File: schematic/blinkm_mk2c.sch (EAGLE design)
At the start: 16 parts, among them CN1 1X4SMT, U1 ATTINY44QFN

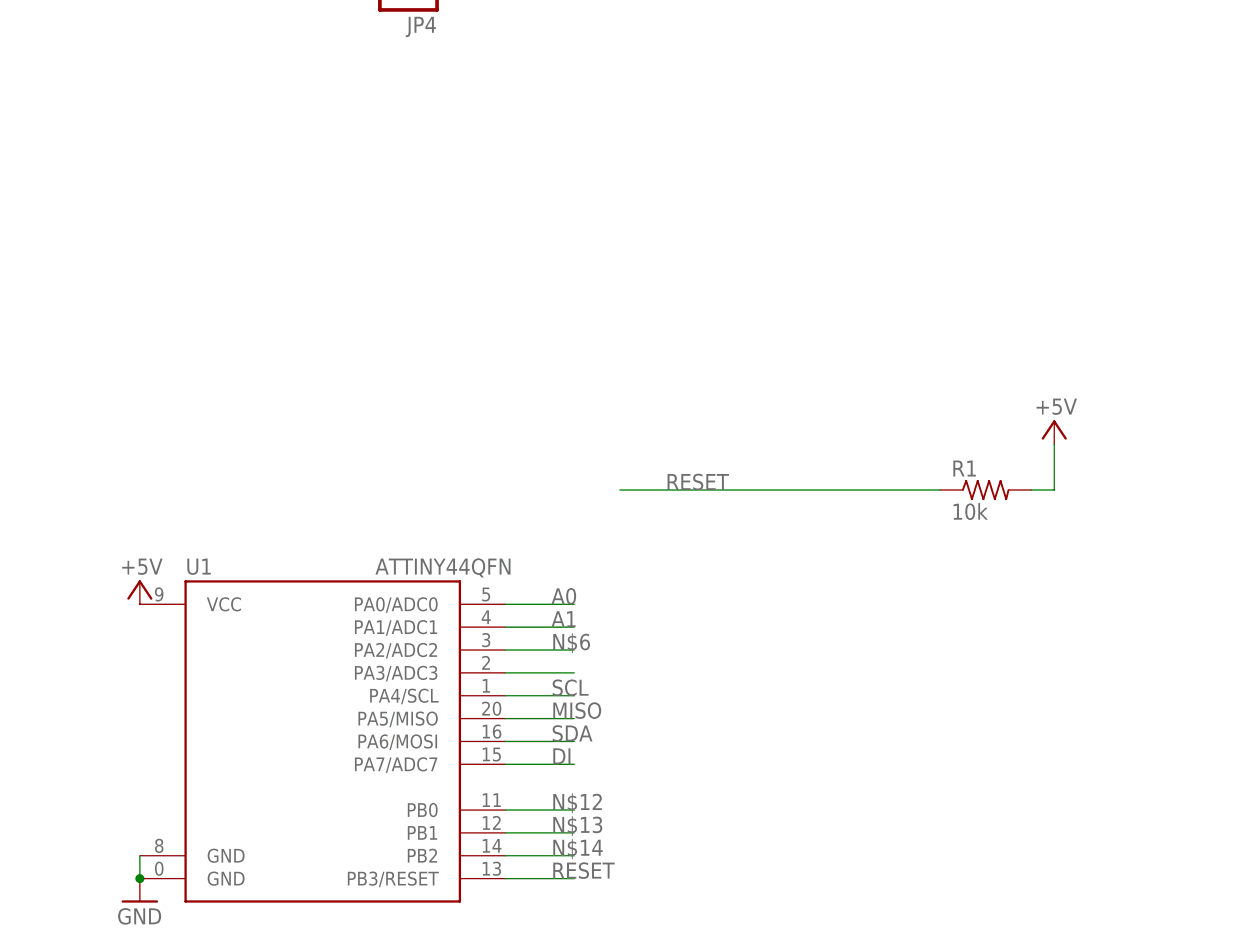
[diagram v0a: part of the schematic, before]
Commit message: updated blinkm_mk2c board layout, fully routed
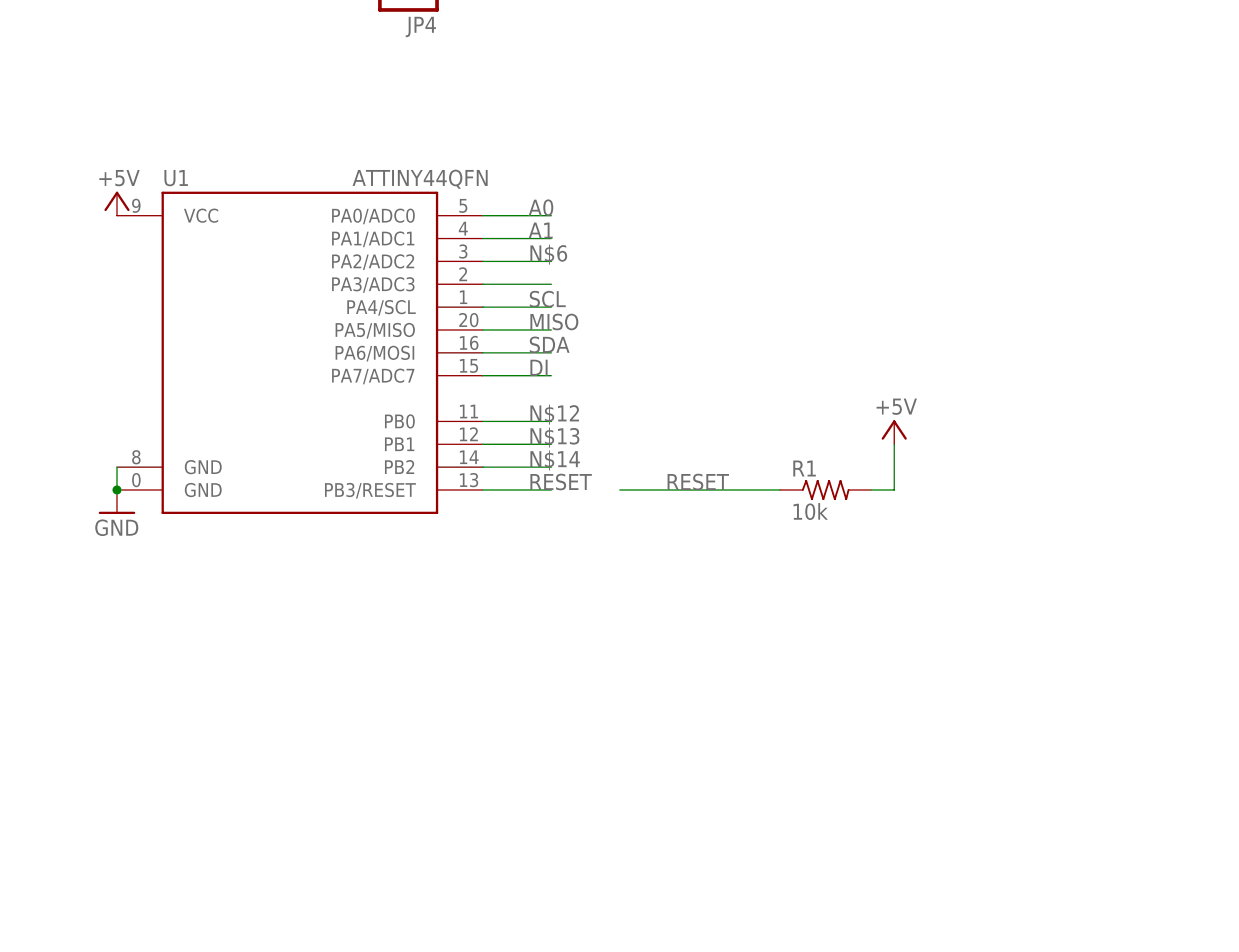
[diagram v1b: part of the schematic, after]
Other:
- moved on the sheet: R1, U1
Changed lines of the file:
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@@
 <instance part="C1" gate="G$1" x="22.86" y="175.26"/>
 <instance part="GND7" gate="1" x="220.98" y="83.82"/>
-<instance part="R1" gate="G$1" x="127" y="71.12"/>
-<instance part="P+3" gate="1" x="134.62" y="78.74" smashed="yes">
-<attribute name="VALUE" x="137.16" y="81.28" size="1.778" layer="96" rot="R180"/>
+<instance part="R1" gate="G$1" x="109.22" y="71.12"/>
+<instance part="P+3" gate="1" x="116.84" y="78.74" smashed="yes">
+<attribute name="VALUE" x="119.38" y="81.28" size="1.778" layer="96" rot="R180"/>
 </instance>
 <instance part="P+4" gate="1" x="35.56" y="187.96" smashed="yes">
@@
 <instance part="JP1" gate="G$1" x="134.62" y="175.26" rot="R180"/>
 <instance part="JP2" gate="G$1" x="134.62" y="154.94" rot="R180"/>
-<instance part="U1" gate="G$1" x="53.34" y="43.18"/>
-<instance part="GND2" gate="1" x="33.02" y="25.4"/>
-<instance part="P+5" gate="1" x="33.02" y="60.96" smashed="yes">
-<attribute name="VALUE" x="35.56" y="63.5" size="1.778" layer="96" rot="R180"/>
+<instance part="U1" gate="G$1" x="50.8" y="86.36"/>
+<instance part="GND2" gate="1" x="30.48" y="68.58"/>
+<instance part="P+5" gate="1" x="30.48" y="104.14" smashed="yes">
+<attribute name="VALUE" x="33.02" y="106.68" size="1.778" layer="96" rot="R180"/>
 </instance>
 </instances>
@@
 <pinref part="GND2" gate="1" pin="GND"/>
 <pinref part="U1" gate="G$1" pin="GND"/>
-<wire x1="33.02" y1="30.48" x2="33.02" y2="27.94" width="0.1524" layer="91"/>
-<junction x="33.02" y="27.94"/>
+<wire x1="30.48" y1="73.66" x2="30.48" y2="71.12" width="0.1524" layer="91"/>
+<junction x="30.48" y="71.12"/>
 </segment>
 </net>
 <net name="+5V" class="0">
 <segment>
-<wire x1="134.62" y1="76.2" x2="134.62" y2="71.12" width="0.1524" layer="91"/>
-<wire x1="132.08" y1="71.12" x2="134.62" y2="71.12" width="0.1524" layer="91"/>
+<wire x1="116.84" y1="76.2" x2="116.84" y2="71.12" width="0.1524" layer="91"/>
+<wire x1="114.3" y1="71.12" x2="116.84" y2="71.12" width="0.1524" layer="91"/>
 <pinref part="P+3" gate="1" pin="+5V"/>
 <pinref part="R1" gate="G$1" pin="2"/>
@@
 <segment>
 <pinref part="U1" gate="G$1" pin="PA7/ADC7"/>
-<wire x1="73.66" y1="40.64" x2="81.28" y2="40.64" width="0.1524" layer="91"/>
-<label x="78.74" y="40.64" size="1.778" layer="95"/>
+<wire x1="71.12" y1="83.82" x2="78.74" y2="83.82" width="0.1524" layer="91"/>
+<label x="76.2" y="83.82" size="1.778" layer="95"/>
 </segment>
 </net>
@@
 <segment>
 <pinref part="U1" gate="G$1" pin="PA6/MOSI"/>
-<wire x1="73.66" y1="43.18" x2="81.28" y2="43.18" width="0.1524" layer="91"/>
-<label x="78.74" y="43.18" size="1.778" layer="95"/>
+<wire x1="71.12" y1="86.36" x2="78.74" y2="86.36" width="0.1524" layer="91"/>
+<label x="76.2" y="86.36" size="1.778" layer="95"/>
 </segment>
 </net>
@@
 <segment>
 <pinref part="U1" gate="G$1" pin="PA4/SCL"/>
-<wire x1="73.66" y1="48.26" x2="81.28" y2="48.26" width="0.1524" layer="91"/>
-<label x="78.74" y="48.26" size="1.778" layer="95"/>
+<wire x1="71.12" y1="91.44" x2="78.74" y2="91.44" width="0.1524" layer="91"/>
+<label x="76.2" y="91.44" size="1.778" layer="95"/>
 </segment>
 </net>
@@
 </segment>
 <segment>
-<wire x1="86.36" y1="71.12" x2="121.92" y2="71.12" width="0.1524" layer="91"/>
+<wire x1="86.36" y1="71.12" x2="104.14" y2="71.12" width="0.1524" layer="91"/>
 <label x="91.44" y="71.12" size="1.778" layer="95"/>
 <pinref part="R1" gate="G$1" pin="1"/>
@@
 <segment>
 <pinref part="U1" gate="G$1" pin="PB3/RESET"/>
-<wire x1="73.66" y1="27.94" x2="81.28" y2="27.94" width="0.1524" layer="91"/>
-<label x="78.74" y="27.94" size="1.778" layer="95"/>
+<wire x1="71.12" y1="71.12" x2="78.74" y2="71.12" width="0.1524" layer="91"/>
+<label x="76.2" y="71.12" size="1.778" layer="95"/>
 </segment>
 </net>
@@
 <segment>
 <pinref part="U1" gate="G$1" pin="PA5/MISO"/>
-<wire x1="73.66" y1="45.72" x2="81.28" y2="45.72" width="0.1524" layer="91"/>
-<label x="78.74" y="45.72" size="1.778" layer="95"/>
+<wire x1="71.12" y1="88.9" x2="78.74" y2="88.9" width="0.1524" layer="91"/>
+<label x="76.2" y="88.9" size="1.778" layer="95"/>
 </segment>
 </net>
@@
 <segment>
 <pinref part="U1" gate="G$1" pin="PA1/ADC1"/>
-<wire x1="73.66" y1="55.88" x2="81.28" y2="55.88" width="0.1524" layer="91"/>
-<label x="78.74" y="55.88" size="1.778" layer="95"/>
+<wire x1="71.12" y1="99.06" x2="78.74" y2="99.06" width="0.1524" layer="91"/>
+<label x="76.2" y="99.06" size="1.778" layer="95"/>
 </segment>
 </net>
@@
 <segment>
 <pinref part="U1" gate="G$1" pin="PA0/ADC0"/>
-<wire x1="73.66" y1="58.42" x2="81.28" y2="58.42" width="0.1524" layer="91"/>
-<label x="78.74" y="58.42" size="1.778" layer="95"/>
+<wire x1="71.12" y1="101.6" x2="78.74" y2="101.6" width="0.1524" layer="91"/>
+<label x="76.2" y="101.6" size="1.778" layer="95"/>
 </segment>
 </net>
@@
 <segment>
 <pinref part="U1" gate="G$1" pin="PA2/ADC2"/>
-<wire x1="73.66" y1="53.34" x2="81.28" y2="53.34" width="0.1524" layer="91"/>
-<label x="78.74" y="53.34" size="1.778" layer="95"/>
+<wire x1="71.12" y1="96.52" x2="78.74" y2="96.52" width="0.1524" layer="91"/>
+<label x="76.2" y="96.52" size="1.778" layer="95"/>
 </segment>
 </net>
@@
 <segment>
 <pinref part="U1" gate="G$1" pin="PA3/ADC3"/>
-<wire x1="73.66" y1="50.8" x2="81.28" y2="50.8" width="0.1524" layer="91"/>
+<wire x1="71.12" y1="93.98" x2="78.74" y2="93.98" width="0.1524" layer="91"/>
 </segment>
 </net>
@@
 <segment>
 <pinref part="U1" gate="G$1" pin="PB0"/>
-<wire x1="73.66" y1="35.56" x2="81.28" y2="35.56" width="0.1524" layer="91"/>
-<label x="78.74" y="35.56" size="1.778" layer="95"/>
+<wire x1="71.12" y1="78.74" x2="78.74" y2="78.74" width="0.1524" layer="91"/>
+<label x="76.2" y="78.74" size="1.778" layer="95"/>
 </segment>
 </net>
@@
 <segment>
 <pinref part="U1" gate="G$1" pin="PB1"/>
-<wire x1="73.66" y1="33.02" x2="81.28" y2="33.02" width="0.1524" layer="91"/>
-<label x="78.74" y="33.02" size="1.778" layer="95"/>
+<wire x1="71.12" y1="76.2" x2="78.74" y2="76.2" width="0.1524" layer="91"/>
+<label x="76.2" y="76.2" size="1.778" layer="95"/>
 </segment>
 </net>
@@
 <segment>
 <pinref part="U1" gate="G$1" pin="PB2"/>
-<wire x1="73.66" y1="30.48" x2="81.28" y2="30.48" width="0.1524" layer="91"/>
-<label x="78.74" y="30.48" size="1.778" layer="95"/>
-</segment>
-</net>
+<wire x1="71.12" y1="73.66" x2="78.74" y2="73.66" width="0.1524" layer="91"/>
+<label x="76.2" y="73.66" size="1.778" layer="95"/>
+</segment>
+</net>
